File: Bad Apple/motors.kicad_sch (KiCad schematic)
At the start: 2 parts, among them U2 L293D, U3 L293D

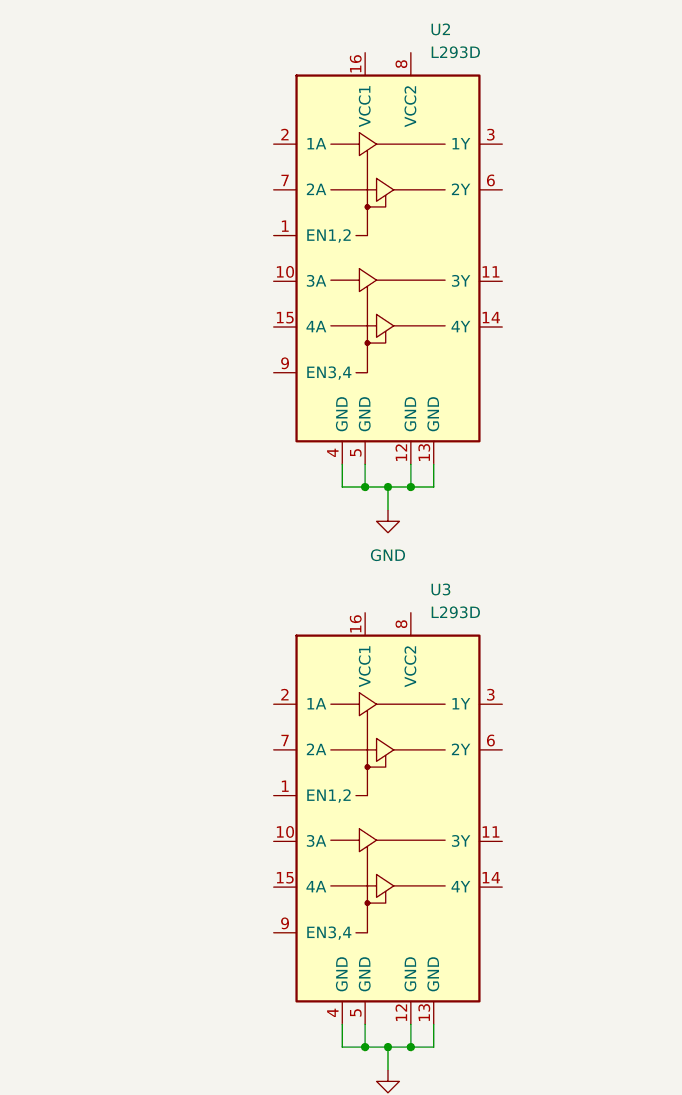
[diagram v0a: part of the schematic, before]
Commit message: feat(pcb): motor subsystem
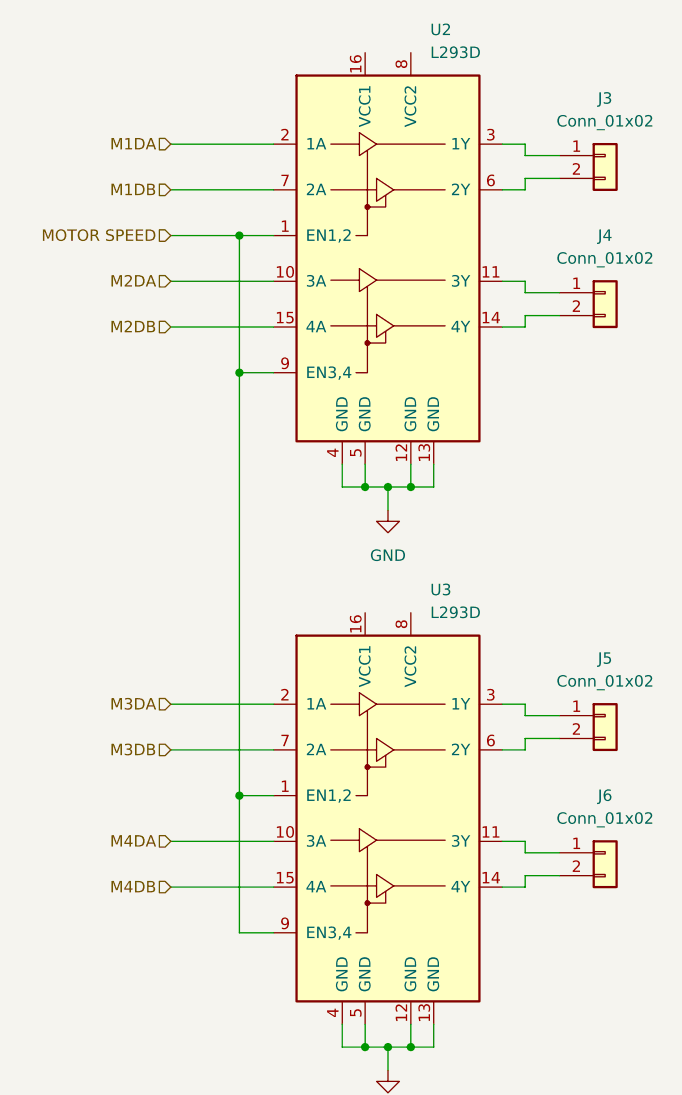
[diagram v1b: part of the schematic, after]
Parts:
- added J3, J4, J5, J6: Conn_01x02, Connector_Wire:SolderWire-0.1sqmm_1x02_P3.6mm_D0.4mm_OD1mm, symbol Connector_Generic:Conn_01x02
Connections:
- net MOTOR SPEED: now reaches U2.1 (EN1,2)
- net MOTOR SPEED: now also U2.9 (EN3,4), U3.1 (EN1,2), U3.9 (EN3,4)
- net M2DA: now reaches U2.10 (3A)
- net at U2.11 (3Y): now also J4.1 (Pin_1)
- net at U2.14 (4Y): now also J4.2 (Pin_2)
- net M2DB: now reaches U2.15 (4A)
- net M1DA: now reaches U2.2 (1A)
- net at U2.3 (1Y): now also J3.1 (Pin_1)
- net at U2.6 (2Y): now also J3.2 (Pin_2)
- net M1DB: now reaches U2.7 (2A)
- net M4DA: now reaches U3.10 (3A)
- net at U3.11 (3Y): now also J6.1 (Pin_1)
- net at U3.14 (4Y): now also J6.2 (Pin_2)
- net M4DB: now reaches U3.15 (4A)
- net M3DA: now reaches U3.2 (1A)
- net at U3.3 (1Y): now also J5.1 (Pin_1)
- net at U3.6 (2Y): now also J5.2 (Pin_2)
- net M3DB: now reaches U3.7 (2A)

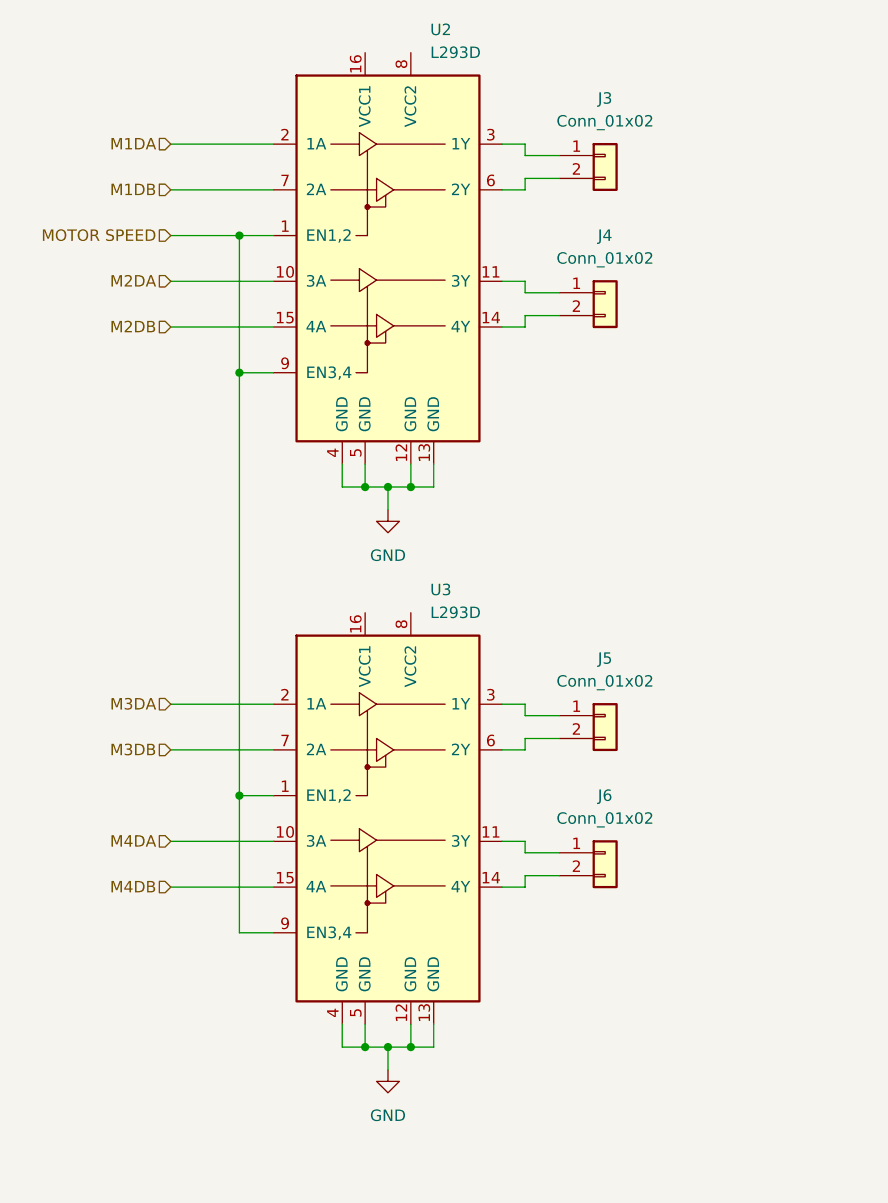
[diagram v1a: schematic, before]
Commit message: feat(pcb): added PCA9685 I2C LED Driver as the driver for the servo motors
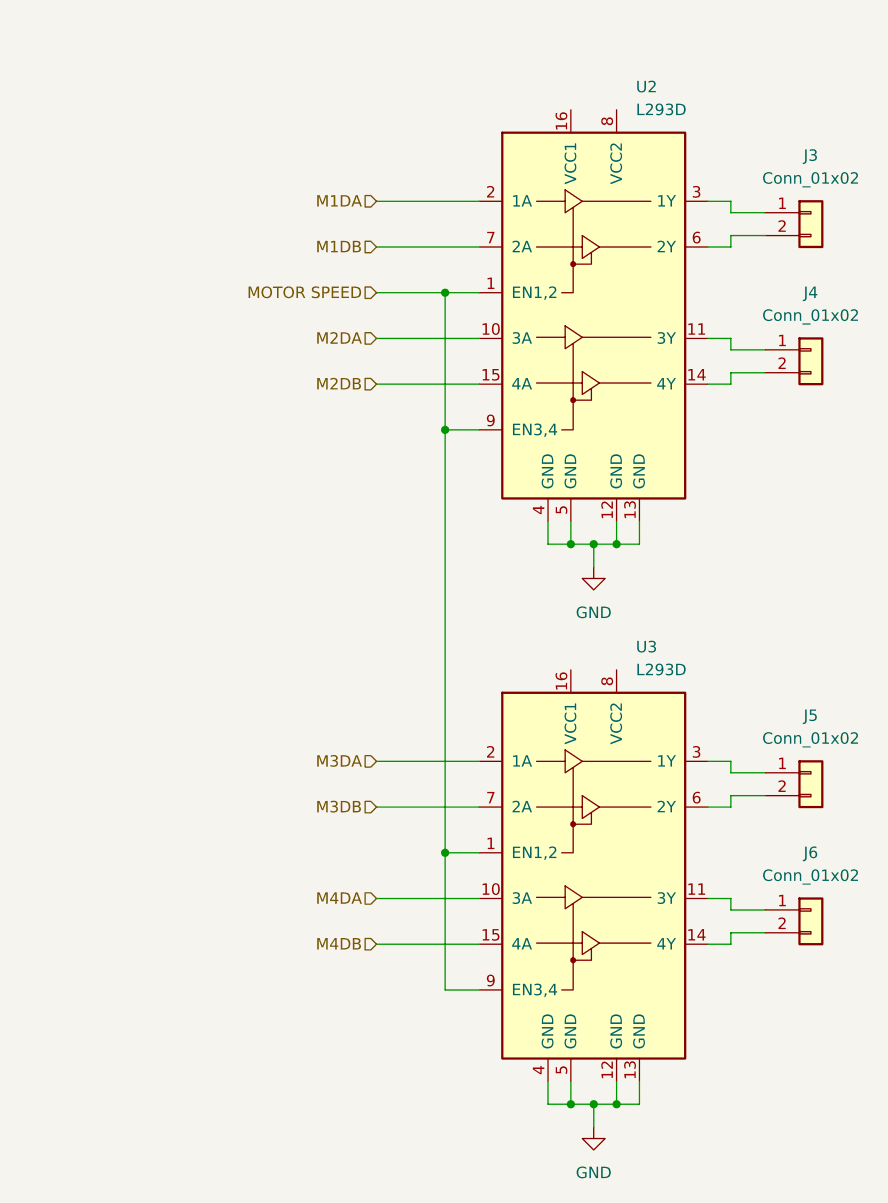
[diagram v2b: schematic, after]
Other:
- moved on the sheet: J3, J4, J5, J6, U2, U3

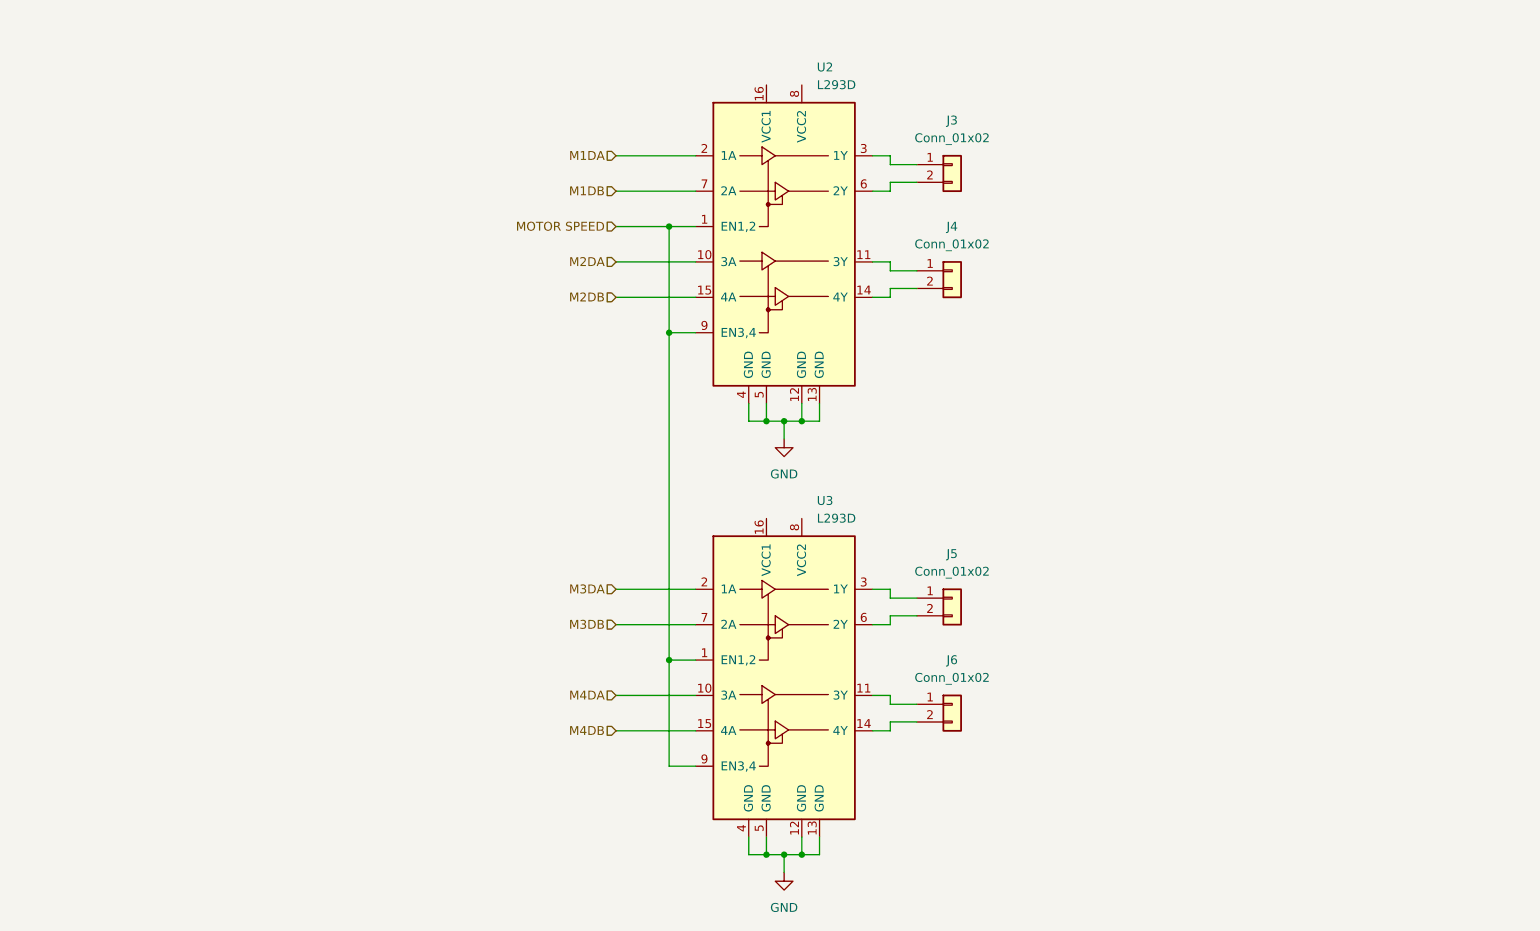
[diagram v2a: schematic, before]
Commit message: feat(pcb): more hierarchy
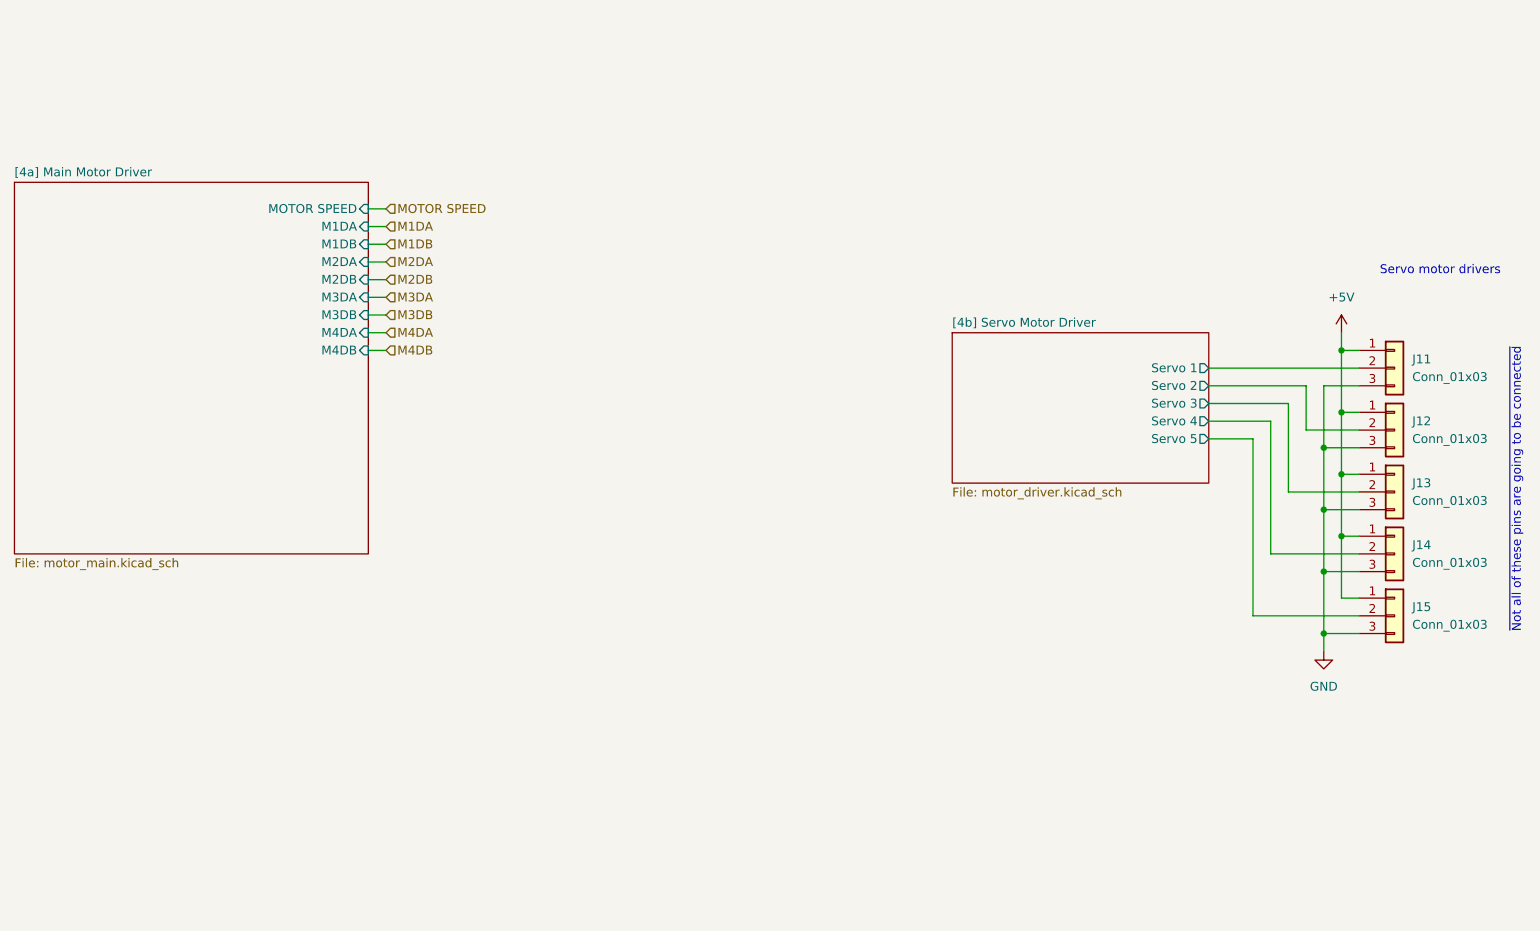
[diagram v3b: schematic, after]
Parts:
- removed J3, J4, J5, J6: Conn_01x02, Connector_Wire:SolderWire-0.1sqmm_1x02_P3.6mm_D0.4mm_OD1mm, symbol Connector_Generic:Conn_01x02
- removed U2, U3: L293D, Package_DIP:DIP-16_W7.62mm, symbol Driver_Motor:L293D
- added J11, J12, J13, J14, J15: Conn_01x03, symbol Connector_Generic:Conn_01x03
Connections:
- net GND: now also J11.3 (Pin_3), J12.3 (Pin_3), J13.3 (Pin_3), J14.3 (Pin_3), J15.3 (Pin_3)
- new net +5V: J11.1 (Pin_1), J12.1 (Pin_1), J13.1 (Pin_1), J14.1 (Pin_1), J15.1 (Pin_1)
- new net [4b] Servo Motor Driver/Servo 1: J11.2 (Pin_2)
- new net [4b] Servo Motor Driver/Servo 2: J12.2 (Pin_2)
- new net [4b] Servo Motor Driver/Servo 3: J13.2 (Pin_2)
- new net [4b] Servo Motor Driver/Servo 4: J14.2 (Pin_2)
- new net [4b] Servo Motor Driver/Servo 5: J15.2 (Pin_2)
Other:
- added sheet [4a] Main Motor Driver (motor_main.kicad_sch)
- added sheet [4b] Servo Motor Driver (motor_driver.kicad_sch)
- note added: "Servo motor drivers"
- note added: "~{Not all of these pins are going to be connected}"
